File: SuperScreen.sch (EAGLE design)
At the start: 30 parts, among them CN1 AMP FCI 10103594-0001LF, CN2 JSTPH, CN3 1X4-BIG, IC2 MIC5225, Q3 BSS138, U2 MCP73831T-2ACI/OT

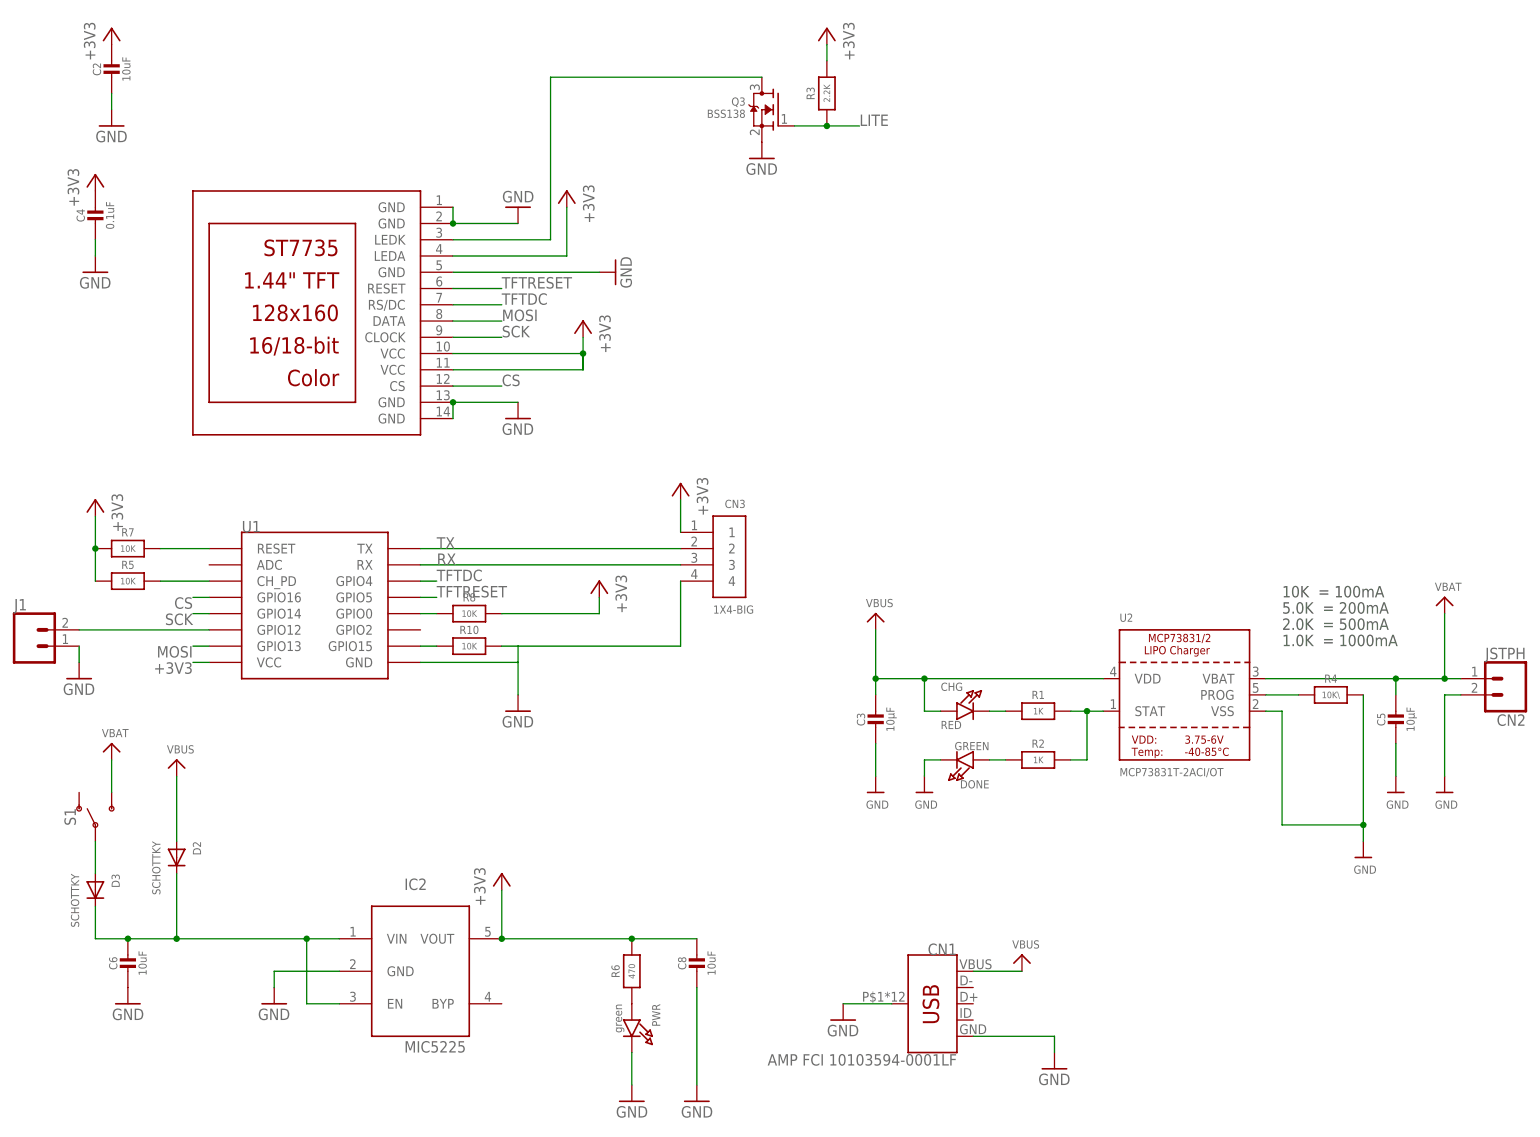
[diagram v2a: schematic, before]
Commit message: Use adafruit's 0805 resistors
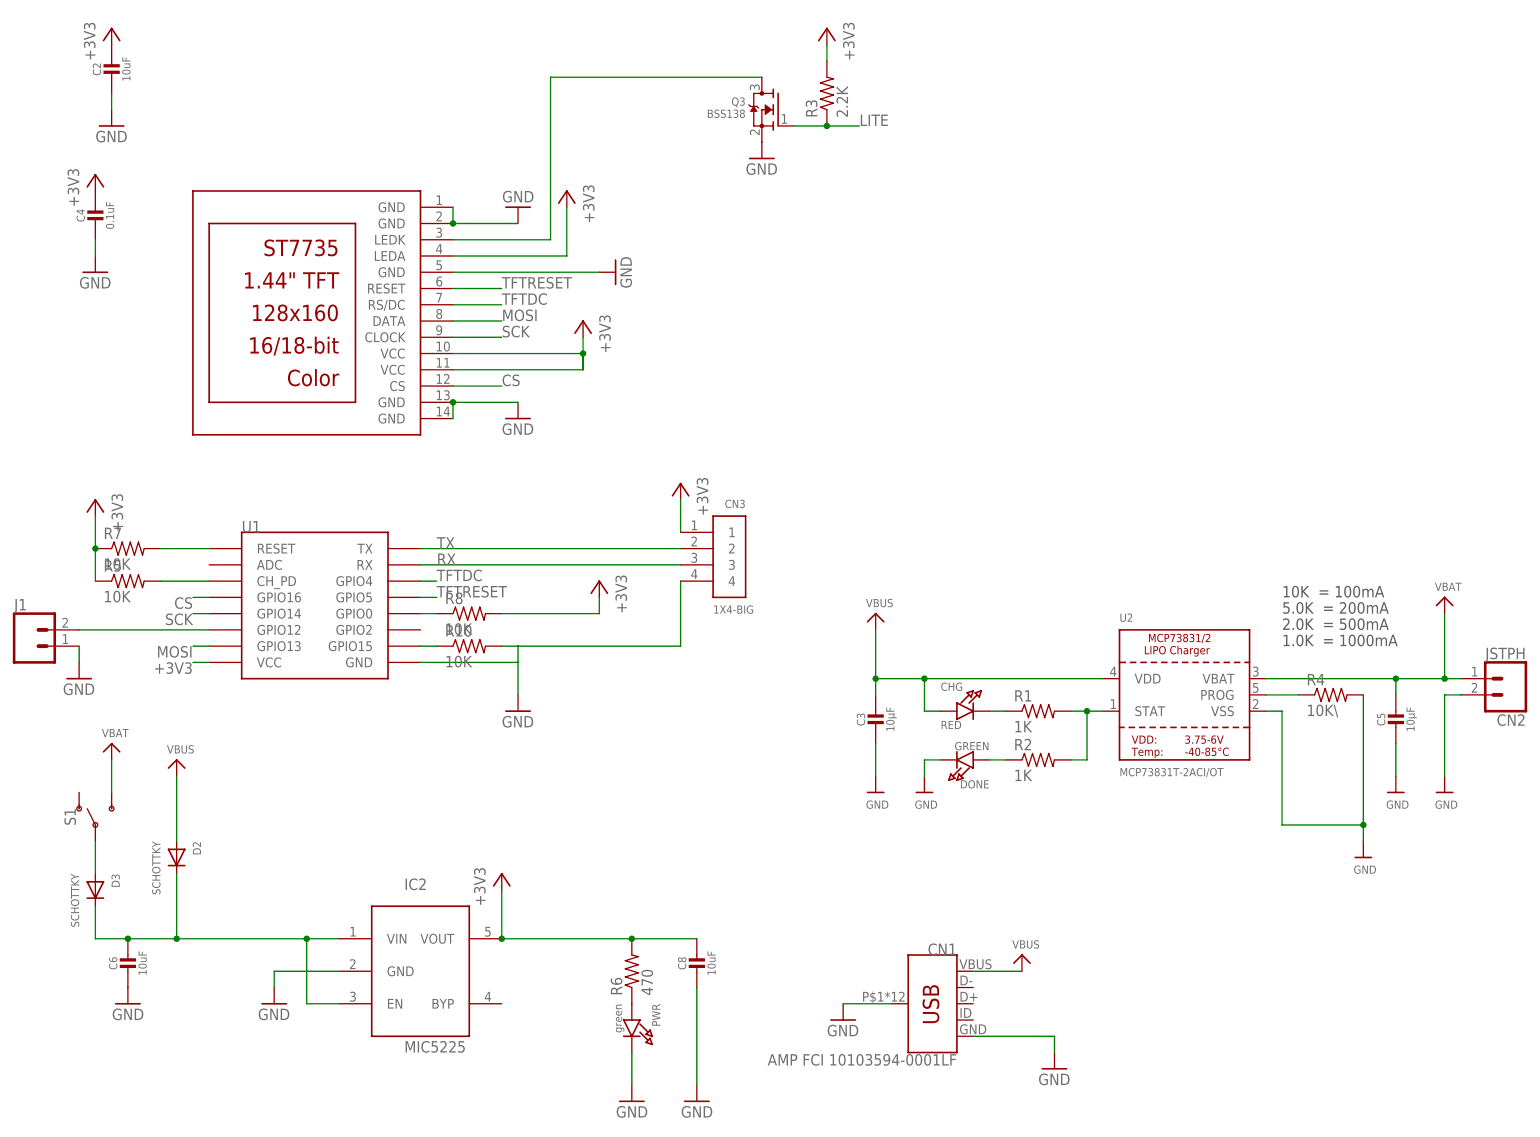
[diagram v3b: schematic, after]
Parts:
- R1, R10, R2, R3, R5, R6, R7, R8: device microbuilder:RESISTOR0805_NOOUTLINE -> adafruit:R-US_R0805
- R4: device microbuilder:RESISTOR_0805MP -> adafruit:R-US_R0805
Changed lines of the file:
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@@
 <?xml version="1.0" encoding="utf-8"?>
 <!DOCTYPE eagle SYSTEM "eagle.dtd">
-<eagle version="8.6.0">
+<eagle version="9.1.2">
 <drawing>
 <settings>
@@
 <grid distance="0.1" unitdist="inch" unit="inch" style="lines" multiple="1" display="no" altdistance="0.01" altunitdist="inch" altunit="inch"/>
 <layers>
-<layer number="1" name="Top" color="4" fill="1" visible="no" active="no"/>
-<layer number="16" name="Bottom" color="1" fill="1" visible="no" active="no"/>
-<layer number="17" name="Pads" color="2" fill="1" visible="no" active="no"/>
-<layer number="18" name="Vias" color="2" fill="1" visible="no" active="no"/>
-<layer number="19" name="Unrouted" color="6" fill="1" visible="no" active="no"/>
-<layer number="20" name="Dimension" color="15" fill="1" visible="no" active="no"/>
-<layer number="21" name="tPlace" color="7" fill="1" visible="no" active="no"/>
-<layer number="22" name="bPlace" color="7" fill="1" visible="no" active="no"/>
-<layer number="23" name="tOrigins" color="15" fill="1" visible="no" active="no"/>
-<layer number="24" name="bOrigins" color="15" fill="1" visible="no" active="no"/>
-<layer number="25" name="tNames" color="7" fill="1" visible="no" active="no"/>
-<layer number="26" name="bNames" color="7" fill="1" visible="no" active="no"/>
-<layer number="27" name="tValues" color="7" fill="1" visible="no" active="no"/>
-<layer number="28" name="bValues" color="7" fill="1" visible="no" active="no"/>
+<layer number="1" name="Top" color="4" fill="1" visible="yes" active="no"/>
+<layer number="16" name="Bottom" color="1" fill="1" visible="yes" active="no"/>
+<layer number="17" name="Pads" color="2" fill="1" visible="yes" active="no"/>
+<layer number="18" name="Vias" color="2" fill="1" visible="yes" active="no"/>
+<layer number="19" name="Unrouted" color="6" fill="1" visible="yes" active="no"/>
+<layer number="20" name="Dimension" color="24" fill="1" visible="yes" active="no"/>
+<layer number="21" name="tPlace" color="7" fill="1" visible="yes" active="no"/>
+<layer number="22" name="bPlace" color="7" fill="1" visible="yes" active="no"/>
+<layer number="23" name="tOrigins" color="15" fill="1" visible="yes" active="no"/>
+<layer number="24" name="bOrigins" color="15" fill="1" visible="yes" active="no"/>
+<layer number="25" name="tNames" color="7" fill="1" visible="yes" active="no"/>
+<layer number="26" name="bNames" color="7" fill="1" visible="yes" active="no"/>
+<layer number="27" name="tValues" color="7" fill="1" visible="yes" active="no"/>
+<layer number="28" name="bValues" color="7" fill="1" visible="yes" active="no"/>
 <layer number="29" name="tStop" color="7" fill="3" visible="no" active="no"/>
 <layer number="30" name="bStop" color="7" fill="6" visible="no" active="no"/>
@@
 <layer number="35" name="tGlue" color="7" fill="4" visible="no" active="no"/>
 <layer number="36" name="bGlue" color="7" fill="5" visible="no" active="no"/>
-<layer number="37" name="tTest" color="7" fill="1" visible="no" active="no"/>
-<layer number="38" name="bTest" color="7" fill="1" visible="no" active="no"/>
+<layer number="37" name="tTest" color="7" fill="1" visible="yes" active="no"/>
+<layer number="38" name="bTest" color="7" fill="1" visible="yes" active="no"/>
 <layer number="39" name="tKeepout" color="4" fill="11" visible="no" active="no"/>
 <layer number="40" name="bKeepout" color="1" fill="11" visible="no" active="no"/>
@@
 <layer number="44" name="Drills" color="7" fill="1" visible="no" active="no"/>
 <layer number="45" name="Holes" color="7" fill="1" visible="no" active="no"/>
-<layer number="46" name="Milling" color="3" fill="1" visible="no" active="no"/>
-<layer number="47" name="Measures" color="7" fill="1" visible="no" active="no"/>
-<layer number="48" name="Document" color="7" fill="1" visible="no" active="no"/>
-<layer number="49" name="Reference" color="7" fill="1" visible="no" active="no"/>
-<layer number="50" name="dxf" color="7" fill="1" visible="no" active="no"/>
-<layer number="51" name="tDocu" color="7" fill="1" visible="no" active="no"/>
-<layer number="52" name="bDocu" color="7" fill="1" visible="no" active="no"/>
-<layer number="53" name="tGND_GNDA" color="7" fill="9" visible="no" active="no"/>
-<layer number="54" name="bGND_GNDA" color="1" fill="9" visible="no" active="no"/>
-<layer number="56" name="wert" color="7" fill="1" visible="no" active="no"/>
-<layer number="57" name="tCAD" color="7" fill="1" visible="no" active="no"/>
-<layer number="59" name="tCarbon" color="7" fill="1" visible="no" active="no"/>
-<layer number="60" name="bCarbon" color="7" fill="1" visible="no" active="no"/>
+<layer number="46" name="Milling" color="3" fill="1" visible="yes" active="no"/>
+<layer number="47" name="Measures" color="7" fill="1" visible="yes" active="no"/>
+<layer number="48" name="Document" color="7" fill="1" visible="yes" active="no"/>
+<layer number="49" name="Reference" color="7" fill="1" visible="yes" active="no"/>
+<layer number="50" name="dxf" color="7" fill="1" visible="yes" active="no"/>
+<layer number="51" name="tDocu" color="7" fill="1" visible="yes" active="no"/>
+<layer number="52" name="bDocu" color="7" fill="1" visible="yes" active="no"/>
+<layer number="53" name="tGND_GNDA" color="7" fill="9" visible="yes" active="no"/>
+<layer number="54" name="bGND_GNDA" color="1" fill="9" visible="yes" active="no"/>
+<layer number="56" name="wert" color="7" fill="1" visible="yes" active="no"/>
+<layer number="57" name="tCAD" color="7" fill="1" visible="yes" active="no"/>
+<layer number="59" name="tCarbon" color="7" fill="1" visible="yes" active="no"/>
+<layer number="60" name="bCarbon" color="7" fill="1" visible="yes" active="no"/>
 <layer number="88" name="SimResults" color="9" fill="1" visible="yes" active="yes"/>
 <layer number="89" name="SimProbes" color="9" fill="1" visible="yes" active="yes"/>
@@
 <part name="GND13" library="supply1" deviceset="GND" device=""/>
 <part name="TFT2" library="microbuilder" deviceset="DISP_LCD_ST7735_1.44IN" device=""/>
-<part name="R3" library="microbuilder" deviceset="RESISTOR" device="0805_NOOUTLINE" value="2.2K"/>
+<part name="R3" library="adafruit" library_urn="urn:adsk.eagle:library:420" deviceset="R-US_" device="R0805" value="2.2K"/>
 <part name="+3V9" library="supply1" deviceset="+3V3" device=""/>
 <part name="Q3" library="microbuilder" deviceset="MOSFET-N" device="WIDE" value="BSS138"/>
@@
 <part name="CHG" library="microbuilder" deviceset="LED" device="0805_NOOUTLINE" value="RED"/>
 <part name="DONE" library="microbuilder" deviceset="LED" device="0805_NOOUTLINE" value="GREEN"/>
-<part name="R1" library="microbuilder" deviceset="RESISTOR" device="0805_NOOUTLINE" value="1K"/>
-<part name="R2" library="microbuilder" deviceset="RESISTOR" device="0805_NOOUTLINE" value="1K"/>
+<part name="R1" library="adafruit" library_urn="urn:adsk.eagle:library:420" deviceset="R-US_" device="R0805" value="1K"/>
+<part name="R2" library="adafruit" library_urn="urn:adsk.eagle:library:420" deviceset="R-US_" device="R0805" value="1K"/>
 <part name="CN2" library="SparkFun-Connectors" library_urn="urn:adsk.eagle:library:513" deviceset="CONN_02" device="" package3d_urn="urn:adsk.eagle:package:38039/1" value="JSTPH"/>
 <part name="C3" library="microbuilder" deviceset="CAP_CERAMIC" device="0805-NOOUTLINE" value="10µF"/>
@@
 <part name="U$4" library="microbuilder" deviceset="GND" device=""/>
 <part name="U$5" library="microbuilder" deviceset="GND" device=""/>
-<part name="R4" library="microbuilder" deviceset="RESISTOR" device="_0805MP" value="10K\"/>
+<part name="R4" library="adafruit" library_urn="urn:adsk.eagle:library:420" deviceset="R-US_" device="R0805" value="10K\"/>
 <part name="U$6" library="microbuilder" deviceset="GND" device=""/>
 <part name="U$7" library="microbuilder" deviceset="GND" device=""/>
@@
 <part name="+3V4" library="supply1" deviceset="+3V3" device=""/>
 <part name="GND10" library="supply1" deviceset="GND" device=""/>
-<part name="R5" library="microbuilder" deviceset="RESISTOR" device="0805_NOOUTLINE" value="10K"/>
-<part name="R7" library="microbuilder" deviceset="RESISTOR" device="0805_NOOUTLINE" value="10K"/>
-<part name="R8" library="microbuilder" deviceset="RESISTOR" device="0805_NOOUTLINE" value="10K"/>
-<part name="R10" library="microbuilder" deviceset="RESISTOR" device="0805_NOOUTLINE" value="10K"/>
+<part name="R5" library="adafruit" library_urn="urn:adsk.eagle:library:420" deviceset="R-US_" device="R0805" value="10K"/>
+<part name="R7" library="adafruit" library_urn="urn:adsk.eagle:library:420" deviceset="R-US_" device="R0805" value="10K"/>
+<part name="R8" library="adafruit" library_urn="urn:adsk.eagle:library:420" deviceset="R-US_" device="R0805" value="10K"/>
+<part name="R10" library="adafruit" library_urn="urn:adsk.eagle:library:420" deviceset="R-US_" device="R0805" value="10K"/>
 <part name="+3V5" library="supply1" deviceset="+3V3" device=""/>
 <part name="CN3" library="adafruit" library_urn="urn:adsk.eagle:library:420" deviceset="1X4" device="-BIG"/>
@@
 <part name="GND12" library="supply1" deviceset="GND" device=""/>
 <part name="S1" library="SparkFun-Switches" library_urn="urn:adsk.eagle:library:535" deviceset="SWITCH-SPDT" device="-SMD-RIGHT-ANGLE" package3d_urn="urn:adsk.eagle:package:40179/1"/>
-<part name="R6" library="microbuilder" deviceset="RESISTOR" device="0805_NOOUTLINE" value="470"/>
+<part name="R6" library="adafruit" library_urn="urn:adsk.eagle:library:420" deviceset="R-US_" device="R0805" value="470"/>
 <part name="GND14" library="supply1" deviceset="GND" device=""/>
 </parts>
